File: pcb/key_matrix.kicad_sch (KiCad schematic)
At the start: 2 parts, among them SW1 SW_Push

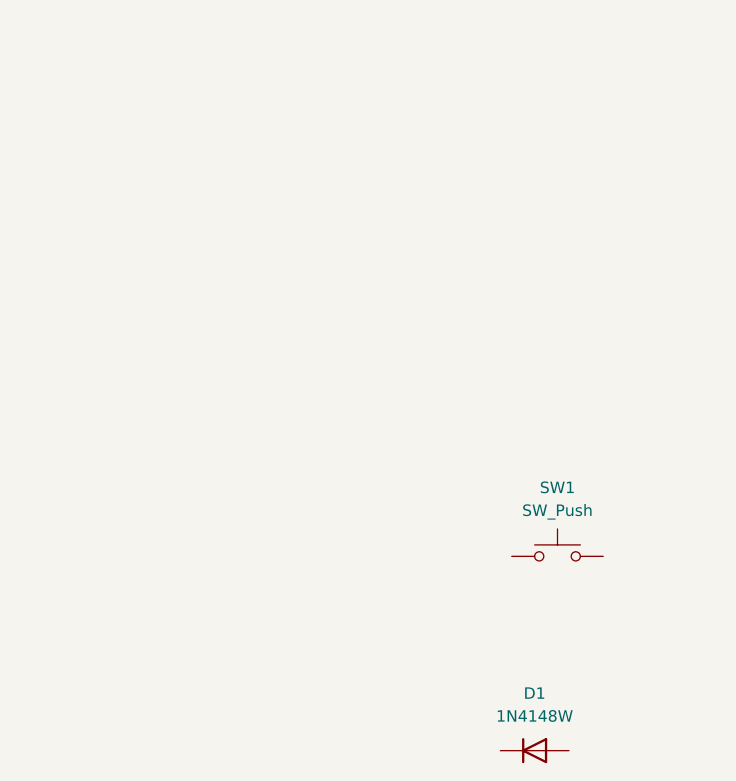
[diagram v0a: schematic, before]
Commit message: feat: place two switch version for testing
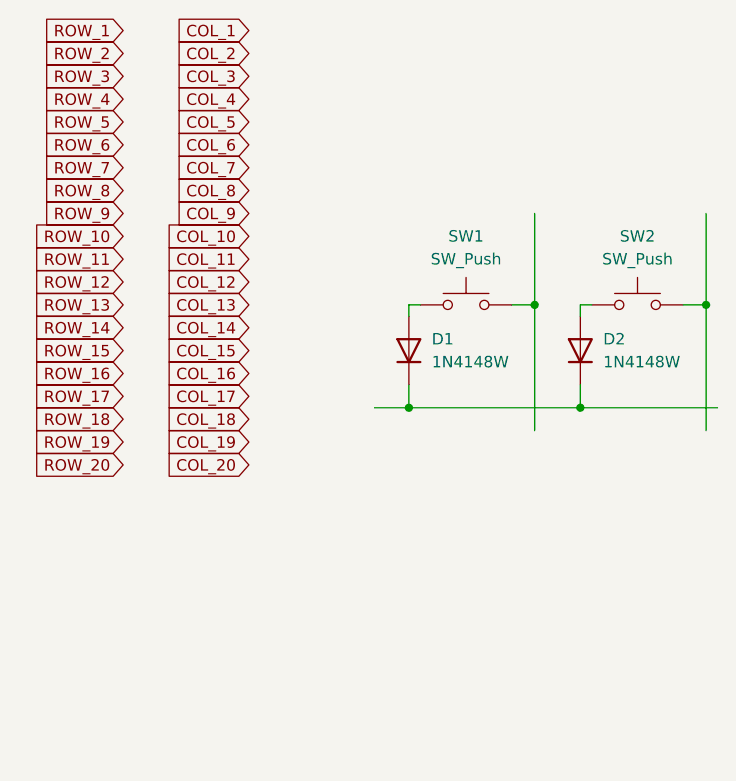
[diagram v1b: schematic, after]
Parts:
- added D2: 1N4148W, Diode_SMD:D_SOD-123, symbol Diode:1N4148W
- added SW2: SW_Push, PCM_Switch_Keyboard_Hotswap_Kailh:SW_Hotswap_Kailh_MX_1.00u, symbol Switch:SW_Push
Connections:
- net at SW1.1: now also D1.2 (A)
- net at D1.1 (K): now also D2.1 (K)
- new net: D2.2 (A), SW2.1
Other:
- moved on the sheet: D1, SW1
